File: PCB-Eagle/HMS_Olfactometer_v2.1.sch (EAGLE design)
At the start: 46 parts, among them IC1 ULQ2803A, IC10 ULQ2803A3, IC3 ULQ2803A, IC4 ULQ2803A, IC5 ULQ2803A, IC6 ULQ2803A, IC8 ULQ2803A

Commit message: [PCB] Modifications to silkscreen
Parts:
- C1: value 7µF -> 6.8µF
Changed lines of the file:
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@@
 <part name="P+21" library="supply1" deviceset="+15V" device=""/>
 <part name="P-4" library="supply1" deviceset="-15V" device=""/>
-<part name="C1" library="rcl" library_urn="urn:adsk.eagle:library:334" deviceset="C-EU" device="C1812" package3d_urn="urn:adsk.eagle:package:23622/2" value="7µF"/>
+<part name="C1" library="rcl" library_urn="urn:adsk.eagle:library:334" deviceset="C-EU" device="C1812" package3d_urn="urn:adsk.eagle:package:23622/2" value="6.8µF"/>
 <part name="GND18" library="SparkFun-Aesthetics" deviceset="GND" device=""/>
 <part name="P+5" library="supply1" deviceset="+12V" device=""/>

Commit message: [PCB] Connect RTS pin to Teensy
The original design (v 2.0) accidentally omitted an RTSpin on the Teensy.
Here I added it into the PCB and made associated changes in the Teensy
code. RTS is on Teensy pin 28, and the rest of the Teensy pin map has
changed accordingly. This pin was chosen to:
- place RTS on the easily accessible pins on the side of the Teensy
- not use up a PWM pin, to keep those for valve driving

In rewiring the PCB, I also added more space around the top left standoff.

This fixes #1 and #4.
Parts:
- U$2: value TEENSY_3.5 -> TEENSY_3.5_ALL_PINS&PADS
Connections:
- net RTS: now also U$2.28
- net V-3WAY-1: now also U$2.37/A18/SCL1/PWM; no longer U$2.36/A17/PWM
- net V-3WAY-2: now also U$2.38/A19/SDA1/PWM; no longer U$2.37/A18/SCL1/PWM
- net V25: now also U$2.29/PWM; no longer U$2.28
- net V26: now also U$2.30/PWM; no longer U$2.29/PWM
- net V27: now also U$2.31/A12/RX4; no longer U$2.30/PWM
- net V28: now also U$2.32/A13/TX4/SCK1; no longer U$2.31/A12/RX4
- net V29: now also U$2.33/A14/TX5; no longer U$2.32/A13/TX4/SCK1
- net V30: now also U$2.34/A15/RX5; no longer U$2.33/A14/TX5
- net V31: now also U$2.35/A16/PWM; no longer U$2.34/A15/RX5
- net V32: now also U$2.36/A17/PWM; no longer U$2.35/A16/PWM
- net V33: now also U$2.39/A20; no longer U$2.38/A19/SDA1/PWM
- net V34: now also U$2.40; no longer U$2.39/A20
- net V35: now also U$2.41; no longer U$2.40
- net V36: now also U$2.42; no longer U$2.41
- net V37: now also U$2.43; no longer U$2.42
- net V38: now also U$2.MOSI2/44; no longer U$2.43
- net V39: now also U$2.MISO2/45; no longer U$2.MOSI2/44
- net V40: now also U$2.SCK2/46; no longer U$2.MISO2/45
- net V41: now also U$2.RX6/47; no longer U$2.SCK2/46
- net V42: now also U$2.TX6/48; no longer U$2.RX6/47
- net V43: now also U$2.A23/49; no longer U$2.TX6/48
- net V44: now also U$2.A24/50; no longer U$2.A23/49
- net V45: now also U$2.51; no longer U$2.A24/50
- net V46: now also U$2.52; no longer U$2.51
- net V47: now also U$2.53; no longer U$2.52
- net V48: now also U$2.54; no longer U$2.53
- net V49: now also U$2.55; no longer U$2.54
- net V50: now also U$2.56; no longer U$2.55
- net V51: now also U$2.57; no longer U$2.56

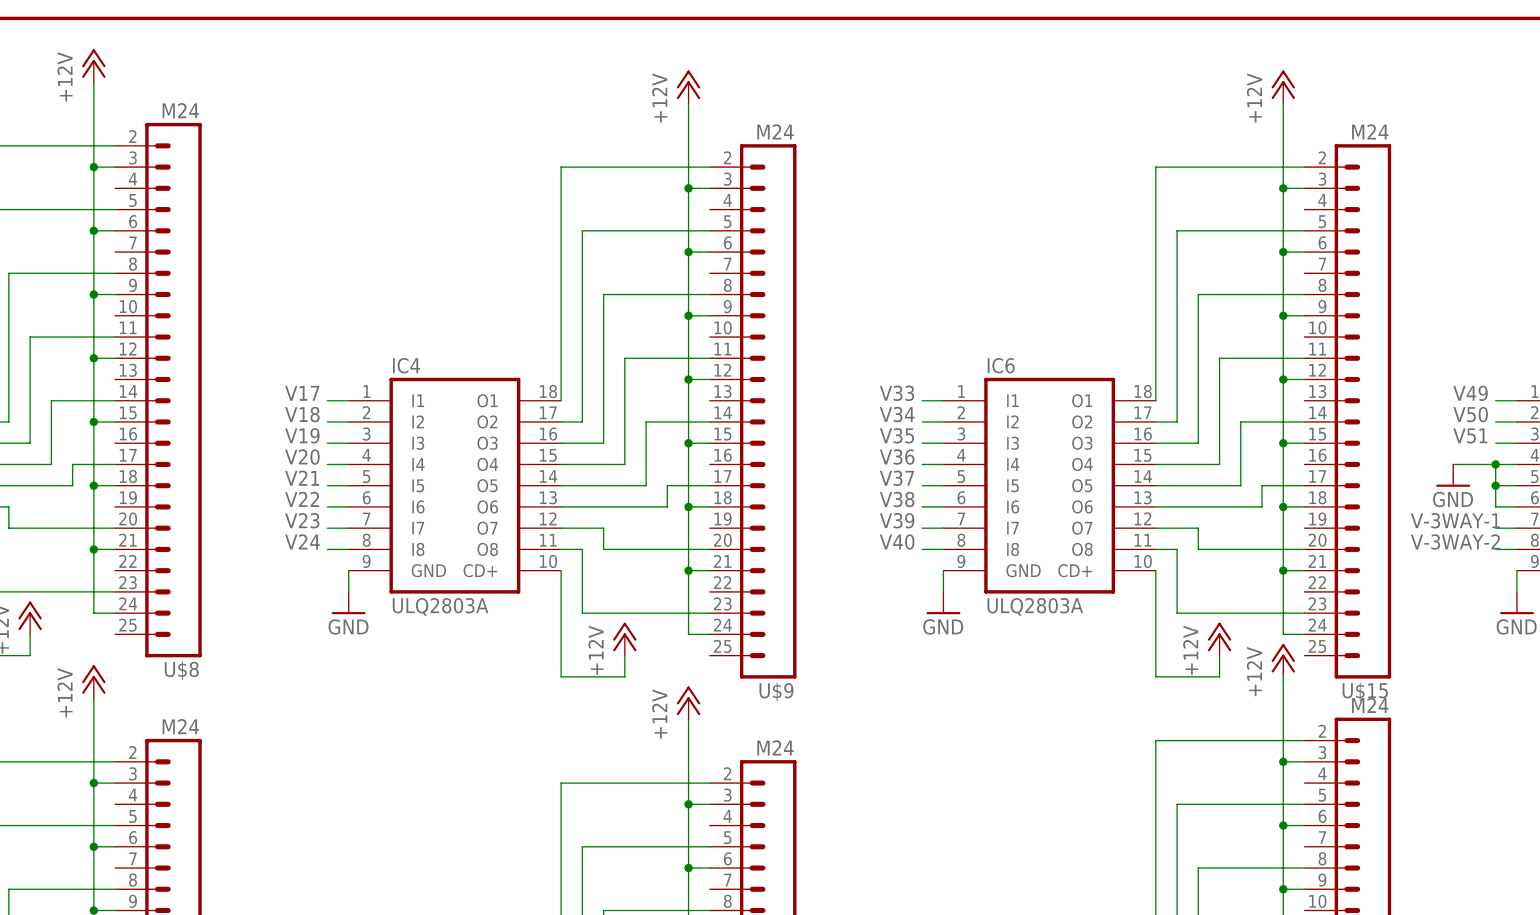
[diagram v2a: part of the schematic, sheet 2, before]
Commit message: [PCB] Update capacitor values; Fix silkscreen and BOM
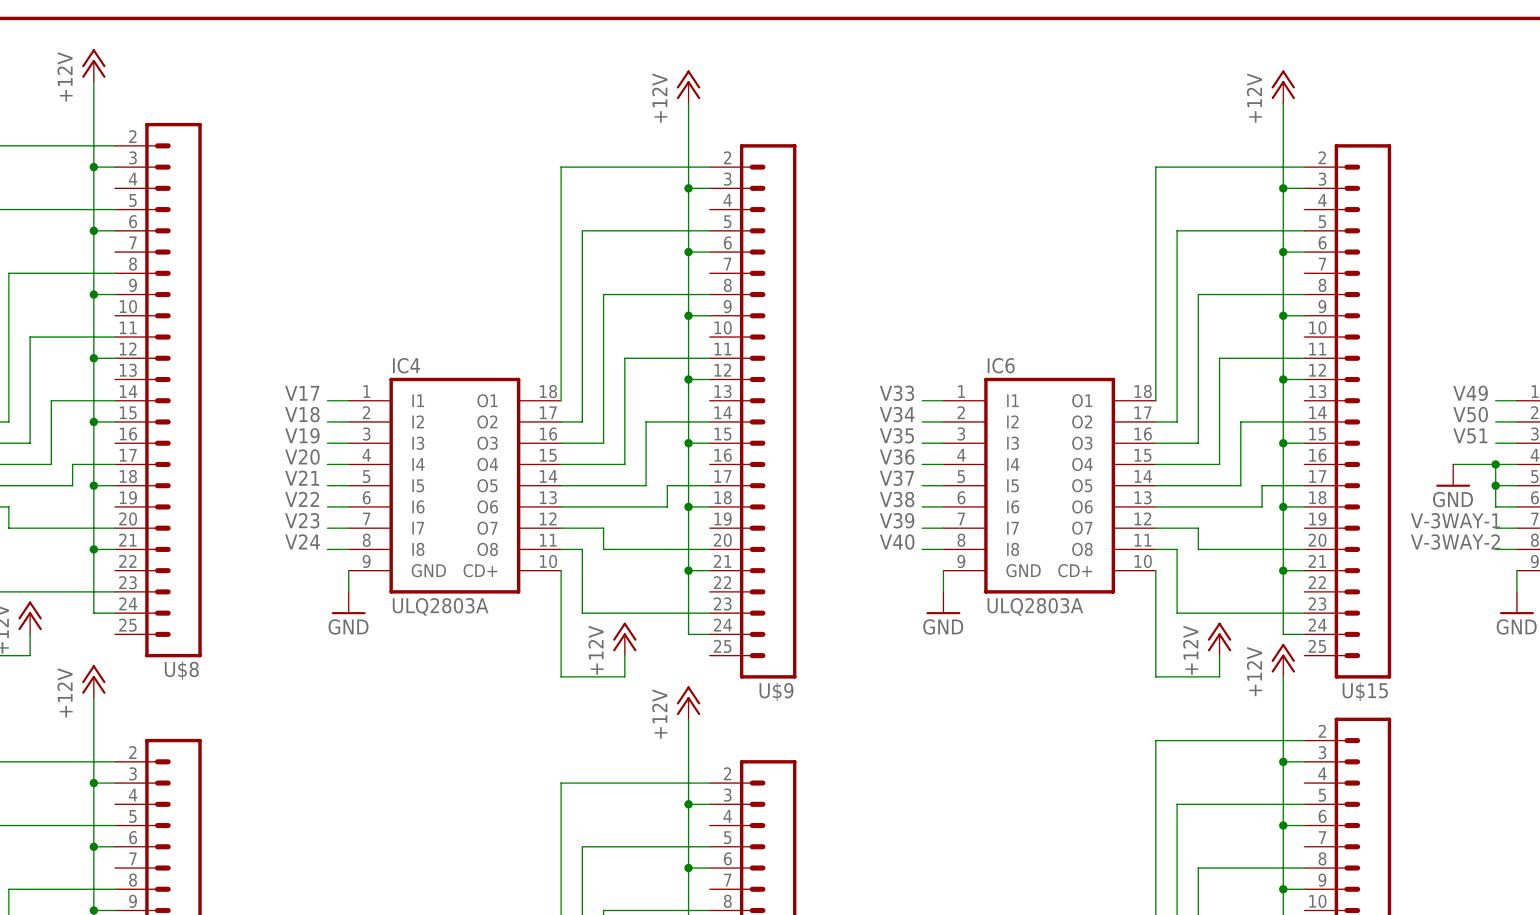
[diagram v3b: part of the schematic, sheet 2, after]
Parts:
- C8: value (none) -> 1uF
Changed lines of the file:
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@@
 <part name="P-2" library="supply1" deviceset="-15V" device=""/>
 <part name="P-3" library="supply1" deviceset="-15V" device=""/>
-<part name="U$8" library="SparkFun-Connectors" deviceset="M24" device=""/>
+<part name="U$8" library="SparkFun-Connectors" deviceset="M24" device="" value=""/>
 <part name="R_A" library="SparkFun-Resistors" deviceset="RESISTOR" device="PTH-1/2W" value="680"/>
 <part name="R_T" library="SparkFun-Resistors" deviceset="RESISTOR" device="PTH-1/2W" value="120"/>
@@
 <part name="C4" library="SparkFun-Capacitors" deviceset="10UF-6.3V-20%(1206)" device="" value="22uF"/>
 <part name="C5" library="SparkFun-Capacitors" deviceset="CAP" device="1206" value="10uF"/>
-<part name="C8" library="SparkFun-Capacitors" deviceset="CAP" device="1206"/>
+<part name="C8" library="SparkFun-Capacitors" deviceset="CAP" device="1206" value="1uF"/>
 <part name="GND16" library="SparkFun-Aesthetics" deviceset="GND" device=""/>
 <part name="GND" library="SparkFun-Connectors" deviceset="M01" device="PTH" value="M01PTH"/>
@@
 <part name="GND12" library="SparkFun-Aesthetics" deviceset="GND" device=""/>
 <part name="P+9" library="supply1" deviceset="+12V" device=""/>
-<part name="U$7" library="SparkFun-Connectors" deviceset="M24" device=""/>
+<part name="U$7" library="SparkFun-Connectors" deviceset="M24" device="" value=""/>
 <part name="P+10" library="supply1" deviceset="+12V" device=""/>
 <part name="IC4" library="uln-udn" deviceset="ULN2803A" device="" value="ULQ2803A"/>
 <part name="GND13" library="SparkFun-Aesthetics" deviceset="GND" device=""/>
 <part name="P+15" library="supply1" deviceset="+12V" device=""/>
-<part name="U$9" library="SparkFun-Connectors" deviceset="M24" device=""/>
+<part name="U$9" library="SparkFun-Connectors" deviceset="M24" device="" value=""/>
 <part name="P+16" library="supply1" deviceset="+12V" device=""/>
 <part name="FRAME2" library="SparkFun-Aesthetics" deviceset="FRAME-LETTER" device=""/>
@@
 <part name="GND14" library="SparkFun-Aesthetics" deviceset="GND" device=""/>
 <part name="P+17" library="supply1" deviceset="+12V" device=""/>
-<part name="U$14" library="SparkFun-Connectors" deviceset="M24" device=""/>
+<part name="U$14" library="SparkFun-Connectors" deviceset="M24" device="" value=""/>
 <part name="P+18" library="supply1" deviceset="+12V" device=""/>
 <part name="IC6" library="uln-udn" deviceset="ULN2803A" device="" value="ULQ2803A"/>
 <part name="GND17" library="SparkFun-Aesthetics" deviceset="GND" device=""/>
 <part name="P+19" library="supply1" deviceset="+12V" device=""/>
-<part name="U$15" library="SparkFun-Connectors" deviceset="M24" device=""/>
+<part name="U$15" library="SparkFun-Connectors" deviceset="M24" device="" value=""/>
 <part name="P+20" library="supply1" deviceset="+12V" device=""/>
 <part name="IC8" library="uln-udn" deviceset="ULN2803A" device="" value="ULQ2803A"/>
 <part name="GND19" library="SparkFun-Aesthetics" deviceset="GND" device=""/>
 <part name="P+23" library="supply1" deviceset="+12V" device=""/>
-<part name="U$17" library="SparkFun-Connectors" deviceset="M24" device=""/>
+<part name="U$17" library="SparkFun-Connectors" deviceset="M24" device="" value=""/>
 <part name="P+24" library="supply1" deviceset="+12V" device=""/>
 <part name="IC10" library="uln-udn" deviceset="ULN2803A" device="" value="ULQ2803A3"/>
